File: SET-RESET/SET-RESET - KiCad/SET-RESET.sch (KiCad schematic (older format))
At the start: 86 parts, among them J1 BMS, J2 BSPD, J3 IMD, J4 IMD_SHTDNW, J5 BMS_SHTDNW, J6 BSPD_SHTDNW, K1 DPST RELAY, K2 DPST RELAY, K3 DPST RELAY, Q1 BC557, Q10 BC548, Q11 BC548, Q12 BC557, Q13 BC548, Q14 BC548, Q15 BC557, Q16 BC548, Q17 BC548, Q18 BC557, Q2 BC557, Q3 BC557, Q4 SI2302, Q5 SI2302, Q6 SI2302, Q7 BC548, Q8 BC548, Q9 BC548, U1 TLP290-4

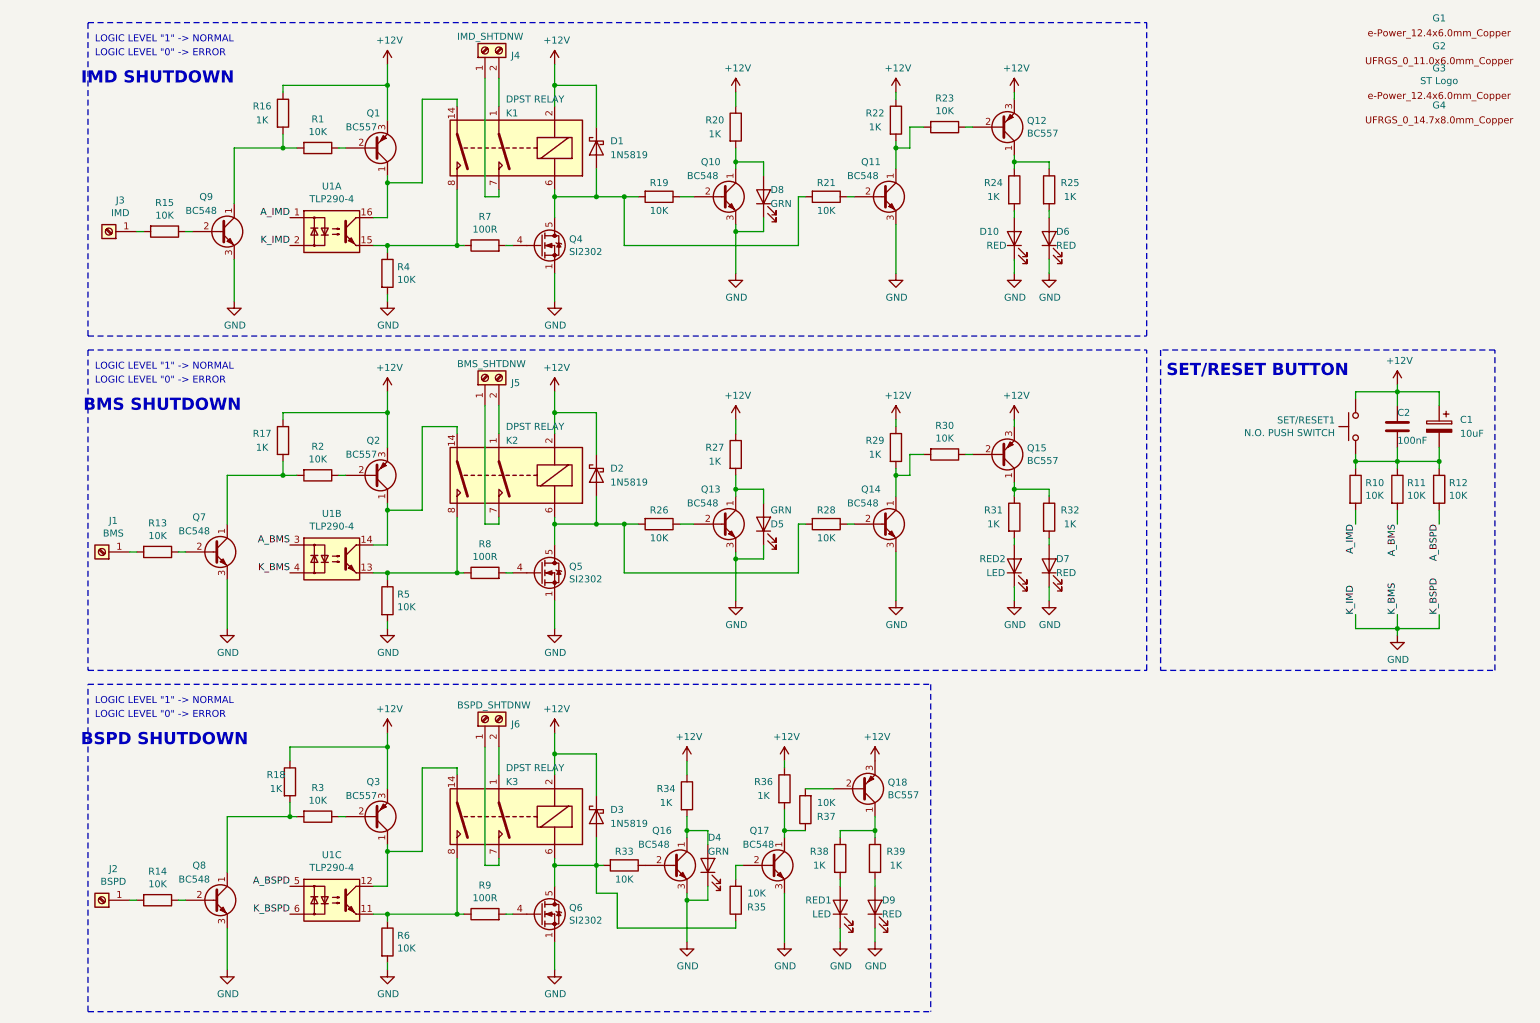
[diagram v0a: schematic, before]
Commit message: Modified SET/RESET circuit. Added BSPD and AIL circuit.
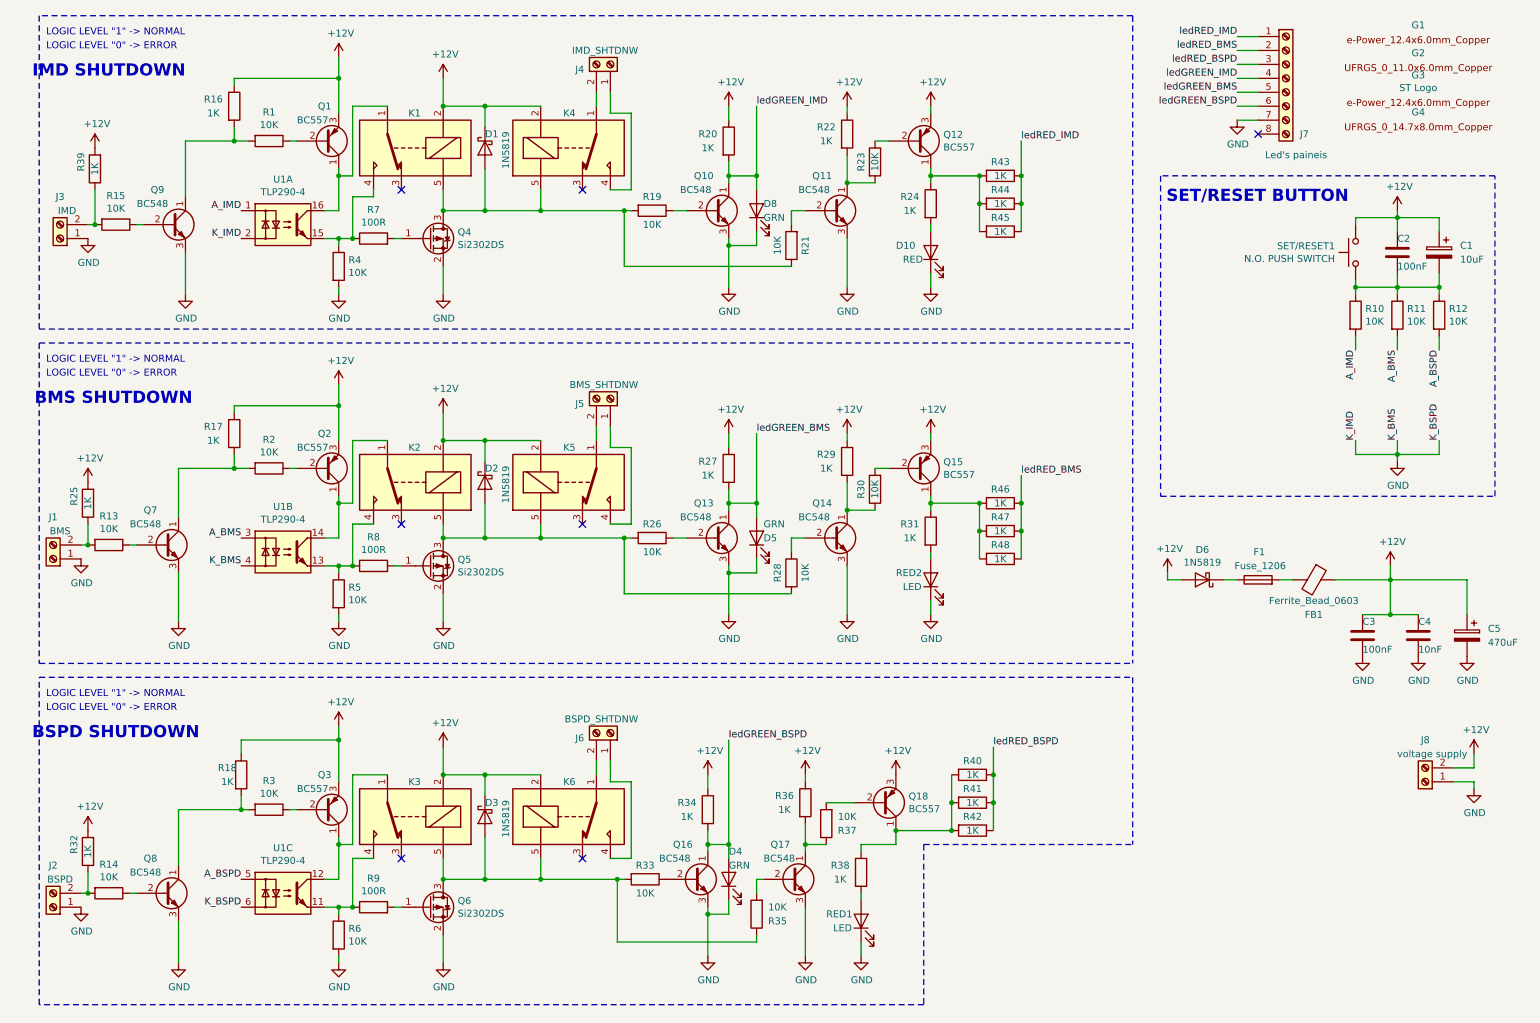
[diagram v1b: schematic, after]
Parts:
- removed D6, D7, D9: RED, LED_THT:LED_D3.0mm, symbol Device:LED
- removed J1: BMS, Connector_PinHeader_1.27mm:PinHeader_1x01_P1.27mm_Vertical, symbol Connector:Screw_Terminal_01x01
- removed J2: BSPD, Connector_PinHeader_1.27mm:PinHeader_1x01_P1.27mm_Vertical, symbol Connector:Screw_Terminal_01x01
- removed J3: IMD, Connector_PinHeader_1.27mm:PinHeader_1x01_P1.27mm_Vertical, symbol Connector:Screw_Terminal_01x01
- removed K1, K2, K3: DPST RELAY, Relay_THT:Relay_StandexMeder_DIP_LowProfile, symbol Relay:DIPxx-2Axx-21x
- removed Q4, Q5, Q6: SI2302, Package_TO_SOT_SMD:SOT-23, symbol Transistor_FET:BUK7M12-40EX
- added C3: 100nF, Capacitor_SMD:C_0603_1608Metric_Pad1.05x0.95mm_HandSolder, symbol Device:C
- added C4: 10nF, Capacitor_SMD:C_0603_1608Metric_Pad1.05x0.95mm_HandSolder, symbol Device:C
- added C5: 470uF, Capacitor_SMD:CP_Elec_4x5.3, symbol Device:CP
- added D6: 1N5819, e-Power:DO-41_SMD, symbol e-Power:1N5819
- added F1: Fuse_1206, e-Power:FUSE_1206_3216Metric, symbol e-Power:Fuse_1206
- added FB1: Ferrite_Bead_0603, e-Power:FB_0603_1608Metric, symbol e-Power:Ferrite_Bead_0603
- added J1: BMS, Connector_Phoenix_GMSTB:PhoenixContact_GMSTBA_2,5_2-G_1x02_P7.50mm_Horizontal, symbol Connector:Screw_Terminal_01x02
- added J2: BSPD, Connector_Phoenix_GMSTB:PhoenixContact_GMSTBA_2,5_2-G_1x02_P7.50mm_Horizontal, symbol Connector:Screw_Terminal_01x02
- added J3: IMD, Connector_Phoenix_GMSTB:PhoenixContact_GMSTBA_2,5_2-G_1x02_P7.50mm_Horizontal, symbol Connector:Screw_Terminal_01x02
- added J7: Led's paineis, Connector_PinHeader_1.27mm:PinHeader_1x08_P1.27mm_Vertical, symbol Connector:Screw_Terminal_01x08
- added J8: voltage supply, Connector_Phoenix_GMSTB:PhoenixContact_GMSTBA_2,5_2-G_1x02_P7.50mm_Horizontal, symbol Connector:Screw_Terminal_01x02
- added K1, K2, K3, K4, K5, K6: RELAY_19.1x15.5mm, e-Power:Relay_SPDT_SANYOU_SRD, symbol e-Power:RELAY_19.1x15.5mm
- added Q4, Q5, Q6: Si2302DS, Package_TO_SOT_SMD:SOT-23, symbol e-Power:Si2302DS
- added R40, R41, R42, R43, R44, R45, R46, R47, R48: 1K, Resistor_SMD:R_1206_3216Metric, symbol Device:R
- D10, RED1, RED2: footprint Connector_PinHeader_2.00mm:PinHeader_1x01_P2.00mm_Vertical -> e-Power:LED_0805_1.15x1.40mm_HandSolder
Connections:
- net +12V: now also R25.2, R32.2, R39.2, C3.1, C4.1, C5.1, D6.2 (A), FB1.1, J8.2 (Pin_2), K1.2, K2.2, K3.2, K4.2, K5.2, K6.2
- net GND: now also C3.2, C4.2, C5.2, J1.1 (Pin_1), J2.1 (Pin_1), J3.1 (Pin_1), J7.7 (Pin_7), J8.1 (Pin_1), Q4.2 (S), Q5.2 (S), Q6.2 (S)
- net at J4.2 (Pin_2): now also K4.1
- net at Q1.1 (C), U1.16: now also K1.1
- net at D1.2 (A), R19.2: now also R21.1, K1.5, K4.5, Q4.3 (D); no longer R21.2
- net at J4.1 (Pin_1): now also K4.4
- net at R4.1, R7.1, U1.15: now also K1.4
- net at R7.2: now also Q4.1 (G)
- net at J5.2 (Pin_2): now also K5.1
- net at Q2.1 (C), U1.14: now also K2.1
- net at D2.2 (A), R26.2, R28.2: now also K2.5, K5.5, Q5.3 (D)
- net at J5.1 (Pin_1): now also K5.4
- net at R5.1, R8.1, U1.13: now also K2.4
- net at R8.2: now also Q5.1 (G)
- net at R13.2: now also R25.1, J1.2 (Pin_2)
- net at J6.2 (Pin_2): now also K6.1
- net at Q3.1 (C), U1.12: now also K3.1
- net at D3.2 (A), R33.2, R35.1: now also K3.5, K6.5, Q6.3 (D)
- net at J6.1 (Pin_1): now also K6.4
- net at R6.1, R9.1, U1.11: now also K3.4
- net at R9.2: now also Q6.1 (G)
- net at R15.2: now also R39.1, J3.2 (Pin_2)
- net ledGREEN_IMD: now reaches D8.2 (A), Q10.1 (C), R20.2
- net ledGREEN_IMD: now also J7.4 (Pin_4)
- net at R14.2: now also R32.1, J2.2 (Pin_2)
- net at Q11.2 (B): now also R21.2; no longer R21.1
- net at Q12.1 (C), R24.1: now also R43.2, R44.2, R45.2; no longer R25.1
- net ledGREEN_BMS: now reaches D5.2 (A), Q13.1 (C), R27.2
- net ledGREEN_BMS: now also J7.5 (Pin_5)
- net at Q14.1 (C), R29.2: now also R30.1; no longer R30.2
- net at Q15.2 (B): now also R30.2; no longer R30.1
- net at Q15.1 (C), R31.1: now also R46.2, R47.2, R48.2; no longer R32.1
- net ledGREEN_BSPD: now reaches D4.2 (A), Q16.1 (C), R34.2
- net ledGREEN_BSPD: now also J7.6 (Pin_6)
- net at Q18.1 (C), R38.1: now also R40.2, R41.2, R42.2; no longer R39.1
- new net: D6.1 (K), F1.1
- new net: F1.2, FB1.2
- new net ledRED_BMS: J7.2 (Pin_2), R46.1, R47.1, R48.1
- new net ledRED_BSPD: J7.3 (Pin_3), R40.1, R41.1, R42.1
- new net ledRED_IMD: J7.1 (Pin_1), R43.1, R44.1, R45.1
- no-connect marks 0 -> 7
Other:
- moved on the sheet: C1, C2, D10, D4, D5, D8, G1, G2, G3, G4, J4, J5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
